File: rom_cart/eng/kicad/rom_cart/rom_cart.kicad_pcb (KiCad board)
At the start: 2 copper layers, 12 parts, among them J1 CONN_ATARI_2600_CART_CARD_2, J2 CONN_A2K6_FLASH_CART_CARD_2, SW1 SW_DIP_x04, SW2 SW_DIP_x04, U1 SST39SF040-70-4C-NHE, U2 74AHCT1G04

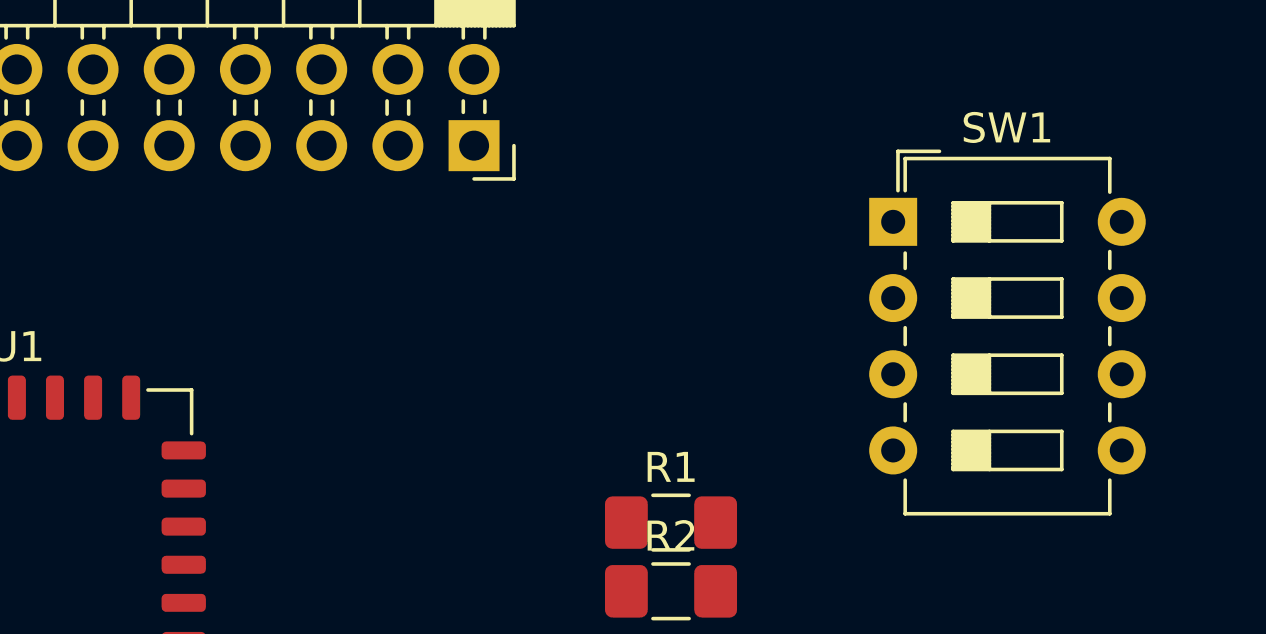
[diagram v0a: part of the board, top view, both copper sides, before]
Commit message: Checked in for backup:-      * Cartridge schematic WIP.      * Connectors PCB socket and card.      * PCB Connector layout WIP.
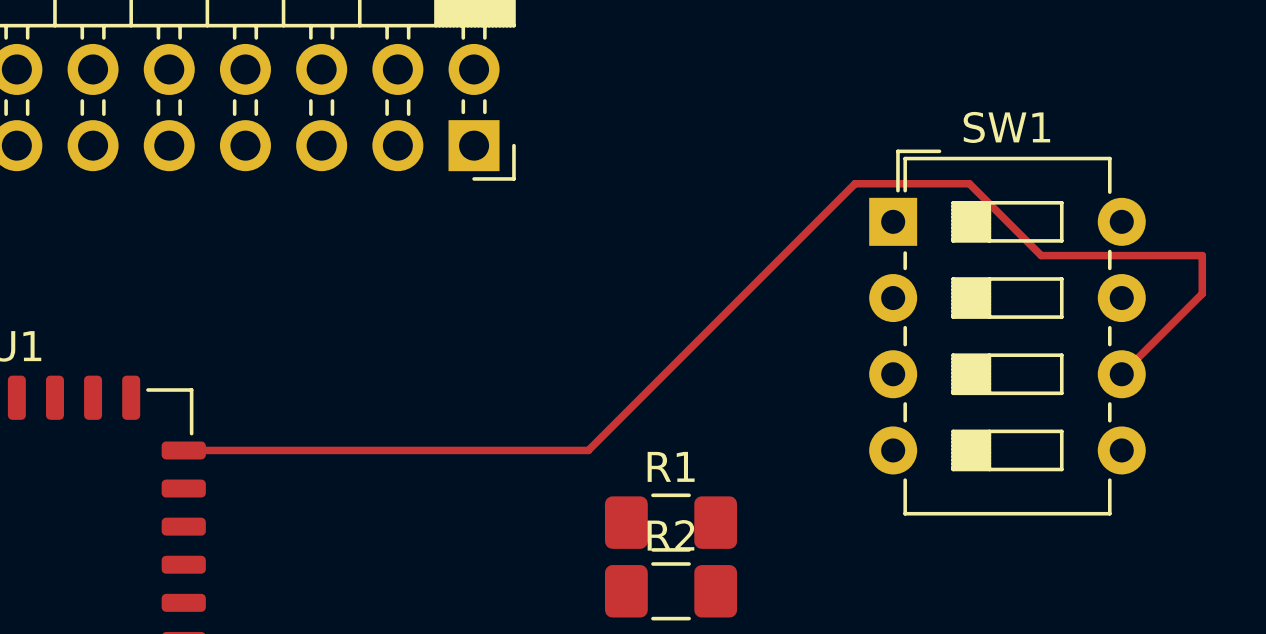
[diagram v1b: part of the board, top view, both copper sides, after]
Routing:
- net /A14: track 0.00 -> 43.7 mm
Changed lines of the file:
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@@
     (thickness 1.6)
     (drawings 0)
-    (tracks 0)
+    (tracks 7)
     (zones 0)
     (modules 12)
@@
     (solder_mask_min_width 0.25)
     (aux_axis_origin 0 0)
-    (visible_elements FFFFFF7F)
+    (visible_elements 7FFFFFFF)
     (pcbplotparams
       (layerselection 0x010fc_ffffffff)
@@
     )
   )
+  (segment (start 147.8025 82.55) (end 161.29 82.55) (width 0.25) (layer F.Cu) (net 58))
+  (segment (start 161.29 82.55) (end 170.18 73.66) (width 0.25) (layer F.Cu) (net 58))
+  (segment (start 170.18 73.66) (end 173.99 73.66) (width 0.25) (layer F.Cu) (net 58))
+  (segment (start 176.385001 76.055001) (end 181.754999 76.055001) (width 0.25) (layer F.Cu) (net 58))
+  (segment (start 173.99 73.66) (end 176.385001 76.055001) (width 0.25) (layer F.Cu) (net 58))
+  (segment (start 181.754999 77.325001) (end 179.07 80.01) (width 0.25) (layer F.Cu) (net 58))
+  (segment (start 181.754999 76.055001) (end 181.754999 77.325001) (width 0.25) (layer F.Cu) (net 58))
 )

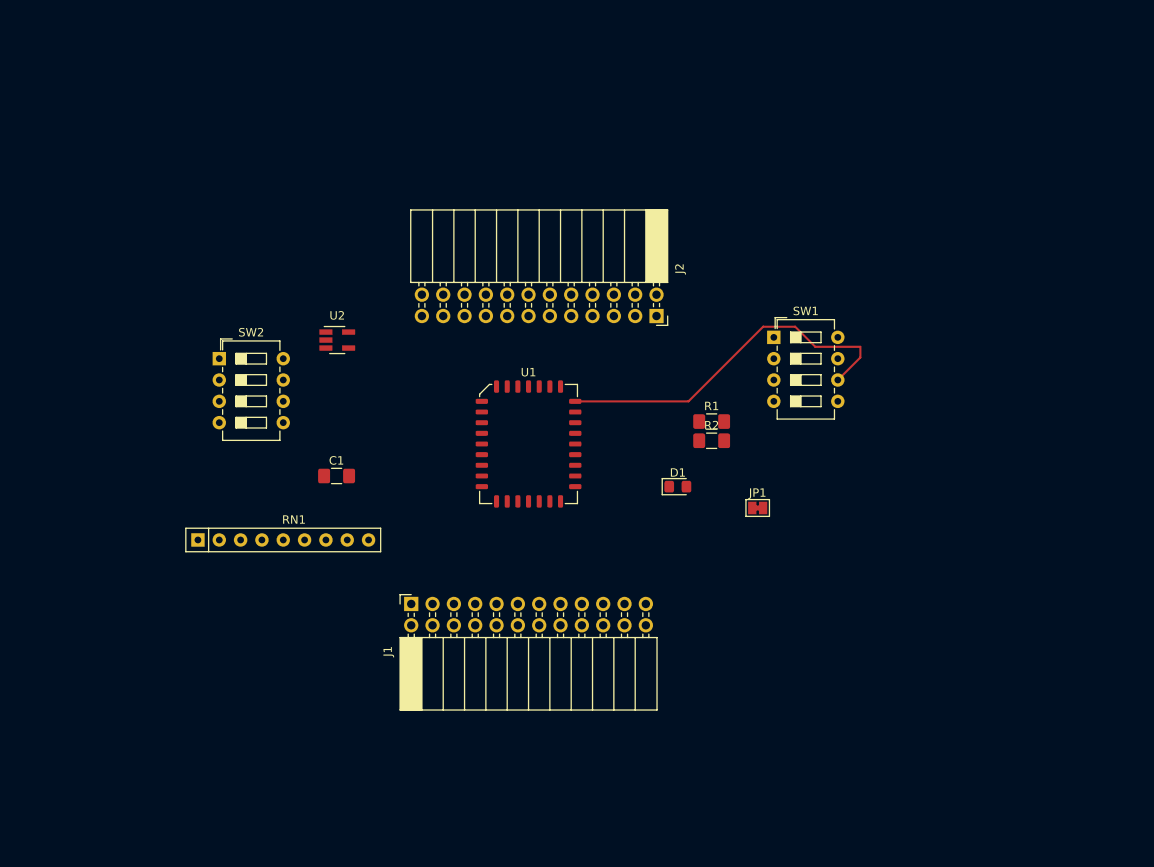
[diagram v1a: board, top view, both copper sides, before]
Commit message: Cartridge schematic nearing completion.
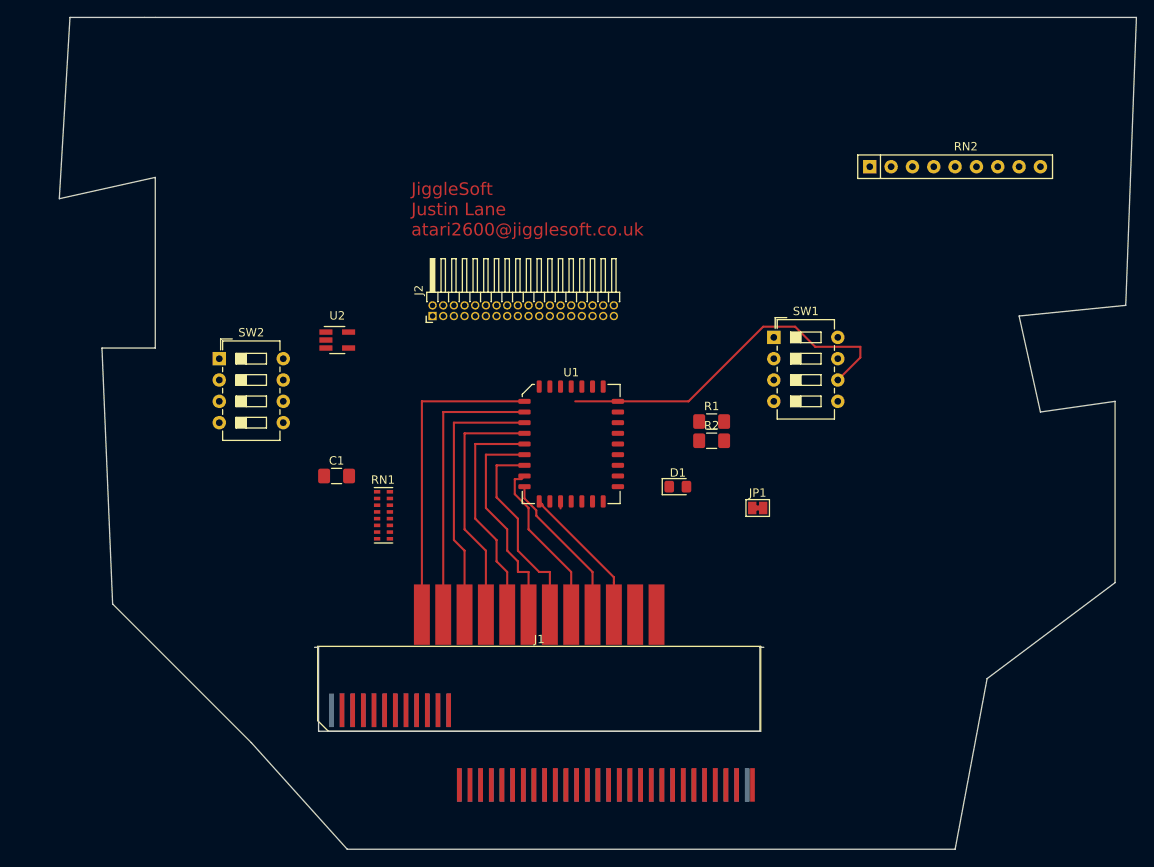
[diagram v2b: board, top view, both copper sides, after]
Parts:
- added RN2: R_Network08, Resistor_THT:R_Array_SIP9, F.Cu at (182.9, 54.6)
- J1: value CONN_ATARI_2600_CART_CARD_2 -> CONN_A2K6_CART_CARD; footprint Connector_PinSocket_2.54mm:PinSocket_2x12_P2.54mm_Horizontal -> JiggleSoft_Conn_Atari:Atari_2600_Cartridge_2x12_PCB_Edge
- J2: value CONN_A2K6_FLASH_CART_CARD_2 -> CONN_512K_CART_CARD; footprint Connector_PinSocket_2.54mm:PinSocket_2x12_P2.54mm_Horizontal -> Connector_PinHeader_1.27mm:PinHeader_2x18_P1.27mm_Horizontal
- RN1: value R_Network08 -> R_Pack08; footprint Resistor_THT:R_Array_SIP9 -> Resistor_SMD:R_Cat16-8
- moved J2 26.7 mm to (130.8, 72.4), turned to 90 degrees
- moved RN1 22.3 mm to (125.0, 96.1)
- moved J1 18.3 mm to (143.5, 116.8), turned to 0 degrees
- moved U1 5.08 mm to (147.3, 87.6)
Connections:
- J2 pad 1: Net-(J2-Pad1) -> /D7
- J2 pad 10: Net-(J2-Pad10) -> /A5
- J2 pad 11: Net-(J2-Pad11) -> /~WE
- J2 pad 12: Net-(J2-Pad12) -> (no net)
- J2 pad 13: Net-(J2-Pad13) -> /A6
- J2 pad 15: Net-(J2-Pad15) -> /A4
- J2 pad 16: Net-(J2-Pad16) -> /A3
- J2 pad 17: Net-(J2-Pad17) -> /A0
- J2 pad 19: Net-(J2-Pad19) -> Net-(J2-Pad18)
- J2 pad 2: Net-(J2-Pad2) -> (no net)
- J2 pad 20: Net-(J2-Pad20) -> /A7
- J2 pad 21: Net-(J2-Pad21) -> /A6
- J2 pad 22: Net-(J2-Pad22) -> /A5
- J2 pad 24: Net-(J2-Pad24) -> /A4
- J2 pad 3: Net-(J2-Pad3) -> /A10
- J2 pad 4: Net-(J2-Pad4) -> /~OE
- J2 pad 5: Net-(J2-Pad5) -> /A11
- J2 pad 6: Net-(J2-Pad6) -> /A9
- J2 pad 7: Net-(J2-Pad7) -> /A8
- J2 pad 8: Net-(J2-Pad8) -> /A1
- J2 pad 9: Net-(J2-Pad9) -> /A2
- RN1 pad 1: GND -> (no net)
- RN1 pad 2: /~OE -> (no net)
- RN1 pad 3: /A18 -> (no net)
- RN1 pad 4: /A17 -> (no net)
- RN1 pad 5: /A16 -> (no net)
- RN1 pad 6: /A15 -> (no net)
- RN1 pad 7: /A14 -> (no net)
- RN1 pad 8: /A13 -> (no net)
- RN1 pad 9: /A12 -> (no net)
- U2 pad 2: /CE -> (no net)
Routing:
- net /A7: track 0.00 -> 37.6 mm
- net /A6: track 0.00 -> 33.8 mm
- net /A5: track 0.00 -> 31.8 mm
- net /A4: track 0.00 -> 30.1 mm
- net /A3: track 0.00 -> 27.8 mm
- net /A2: track 0.00 -> 26.5 mm
- net /A1: track 0.00 -> 24.5 mm
- net /A0: track 0.00 -> 20.2 mm
- net /D0: track 0.00 -> 18.6 mm
- net /D1: track 0.00 -> 17.2 mm
- net GND: track 0.00 -> 0.84 mm
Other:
- board outline added: 128.3 x 99.1 mm
- board text added: "JiggleSoft Justin Lane atari2600@jigglesoft.co.uk"

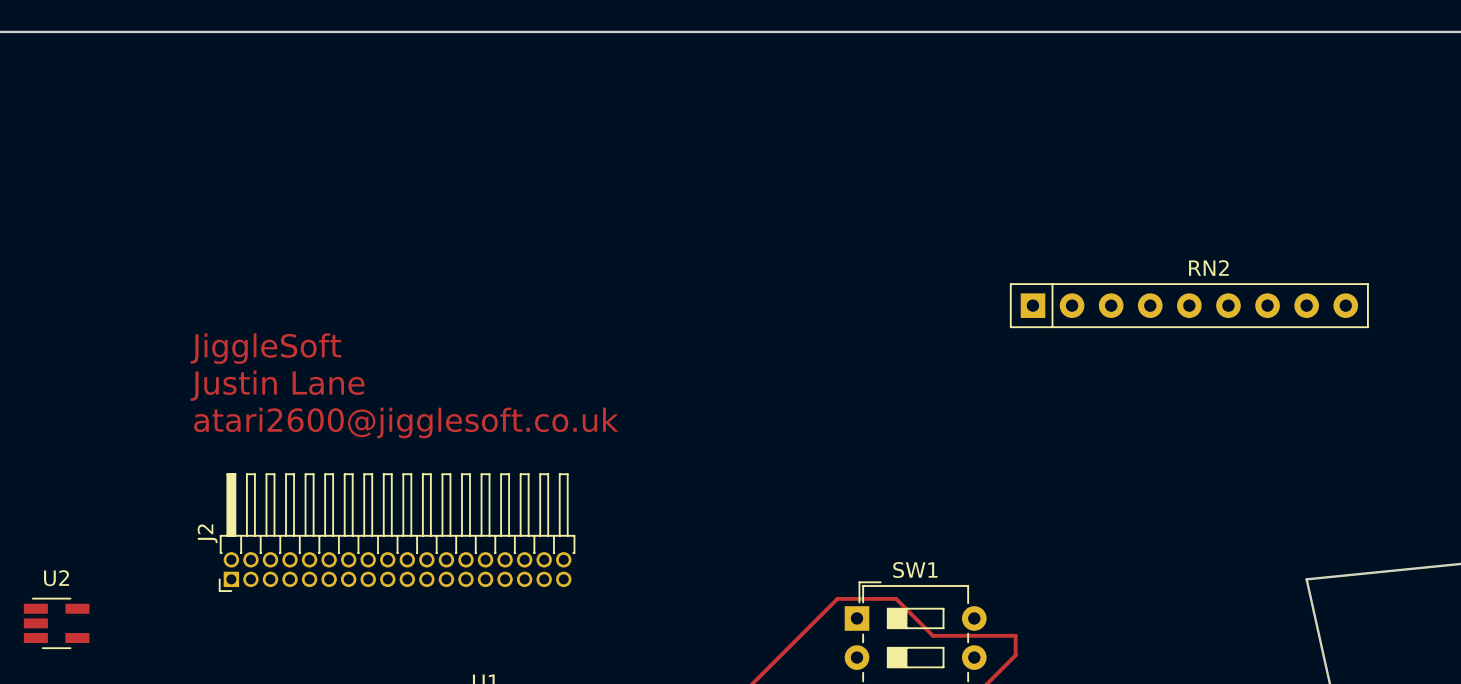
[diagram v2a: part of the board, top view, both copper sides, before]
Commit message: Atari 2600 Budget ROM Cartridge candidate schematic.
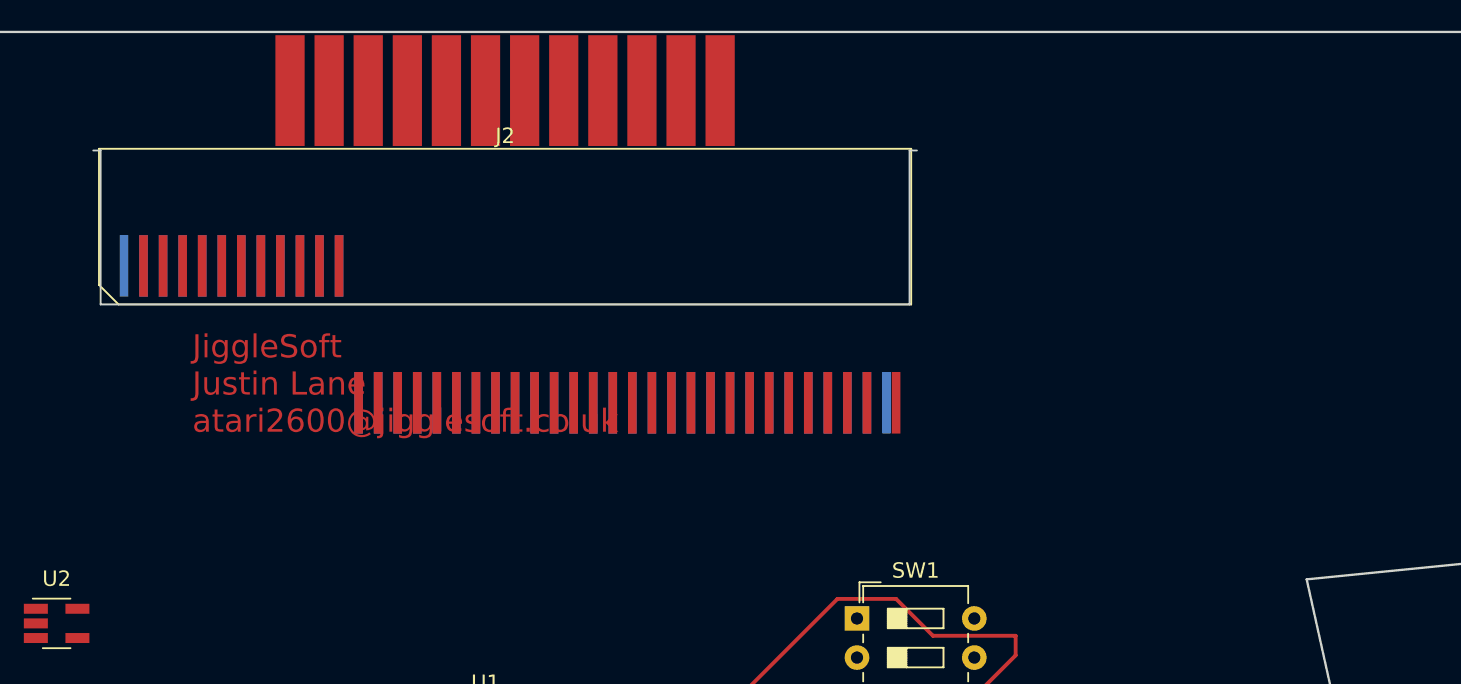
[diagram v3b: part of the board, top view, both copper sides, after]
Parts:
- removed RN2: R_Network08, Resistor_THT:R_Array_SIP9
- J2: footprint Connector_PinHeader_1.27mm:PinHeader_2x18_P1.27mm_Horizontal -> JiggleSoft_Conn_Atari:Atari_2600_Cartridge_2x12_PCB_Edge
- moved J2 29.0 mm to (148.6, 49.5), turned to 0 degrees
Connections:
- J1 pad 12: Net-(J1-Pad12) -> GND
- J1 pad 23: Net-(J1-Pad23) -> +5V
- J1 pad 24: Net-(J1-Pad12) -> GND
- J2 pad 10: /A5 -> /A17
- J2 pad 12: (no net) -> +5V
- J2 pad 13: /A6 -> /A18
- J2 pad 15: /A4 -> /A16
- J2 pad 16: /A3 -> /A15
- J2 pad 17: /A0 -> /A12
- J2 pad 2: (no net) -> /CS
- J2 pad 32: (no net) -> GND
- J2 pad 8: /A1 -> /A13
- J2 pad 9: /A2 -> /A14
- RN1 pad 1: (no net) -> Net-(RN1-Pad1)
- RN1 pad 10: (no net) -> /A18
- RN1 pad 11: (no net) -> /A17
- RN1 pad 12: (no net) -> /A16
- RN1 pad 13: (no net) -> /A15
- RN1 pad 14: (no net) -> /A14
- RN1 pad 15: (no net) -> /A13
- RN1 pad 16: (no net) -> /A12
- RN1 pad 2: (no net) -> Net-(RN1-Pad1)
- RN1 pad 3: (no net) -> Net-(RN1-Pad1)
- RN1 pad 4: (no net) -> Net-(RN1-Pad1)
- RN1 pad 5: (no net) -> Net-(RN1-Pad1)
- RN1 pad 6: (no net) -> Net-(RN1-Pad1)
- RN1 pad 7: (no net) -> Net-(RN1-Pad1)
- RN1 pad 8: (no net) -> GND
- RN1 pad 9: (no net) -> /~OE
- U2 pad 2: (no net) -> /CS
